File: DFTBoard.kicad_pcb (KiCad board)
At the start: 8 copper layers, 148.5 x 62 mm, 294 parts, among them CON1 AVR-JTAG-10, J1 PJ-102A, J2 AUDIO JACK, J3 AUDIO JACK, J4 AUDIO JACK, J5 JACK_TRS_4PINS, J6 USB_A, J7 USB_B, J8 Micro_SD_Card_Det, J9 HDMI_A, Q1 IRLML2502, Q10 IRLML2502, Q2 IRLML2502, Q3 IRLML2502, Q4 IRLML2502, Q5 IRLML2502, Q6 IRLML2502, Q7 IRLML2502, Q8 IRLML2502, Q9 IRLML2502, SW1 TL6215RF200BDT, U1 LM3880, U10 USB3320, U11 MIC2025-1YMM, U12 USB3320, U13 VL53L0X, U14 APDS-9960, U15 MT41K256M16HA-125_E, U16 MT41K256M16HA-125_E, U17 FTDITypeUART, U18 ABRACON-ASDMB, U19 S25FL256SAGNFI001, U2 LM3880, U20 xc7z020clg484, U3 SC189 - 1.0V, U4 SC189 - 3.3V, U5 TLV62080DSGx, U6 LM1085-5.0, U7 SC189 - 1.8V, U8 TPS51200DRCR, U9 TLV320AIC3104, Y1 ABM3-24.000MHZ-D2Y-T, Y2 ABM3-24.000MHZ-D2Y-T

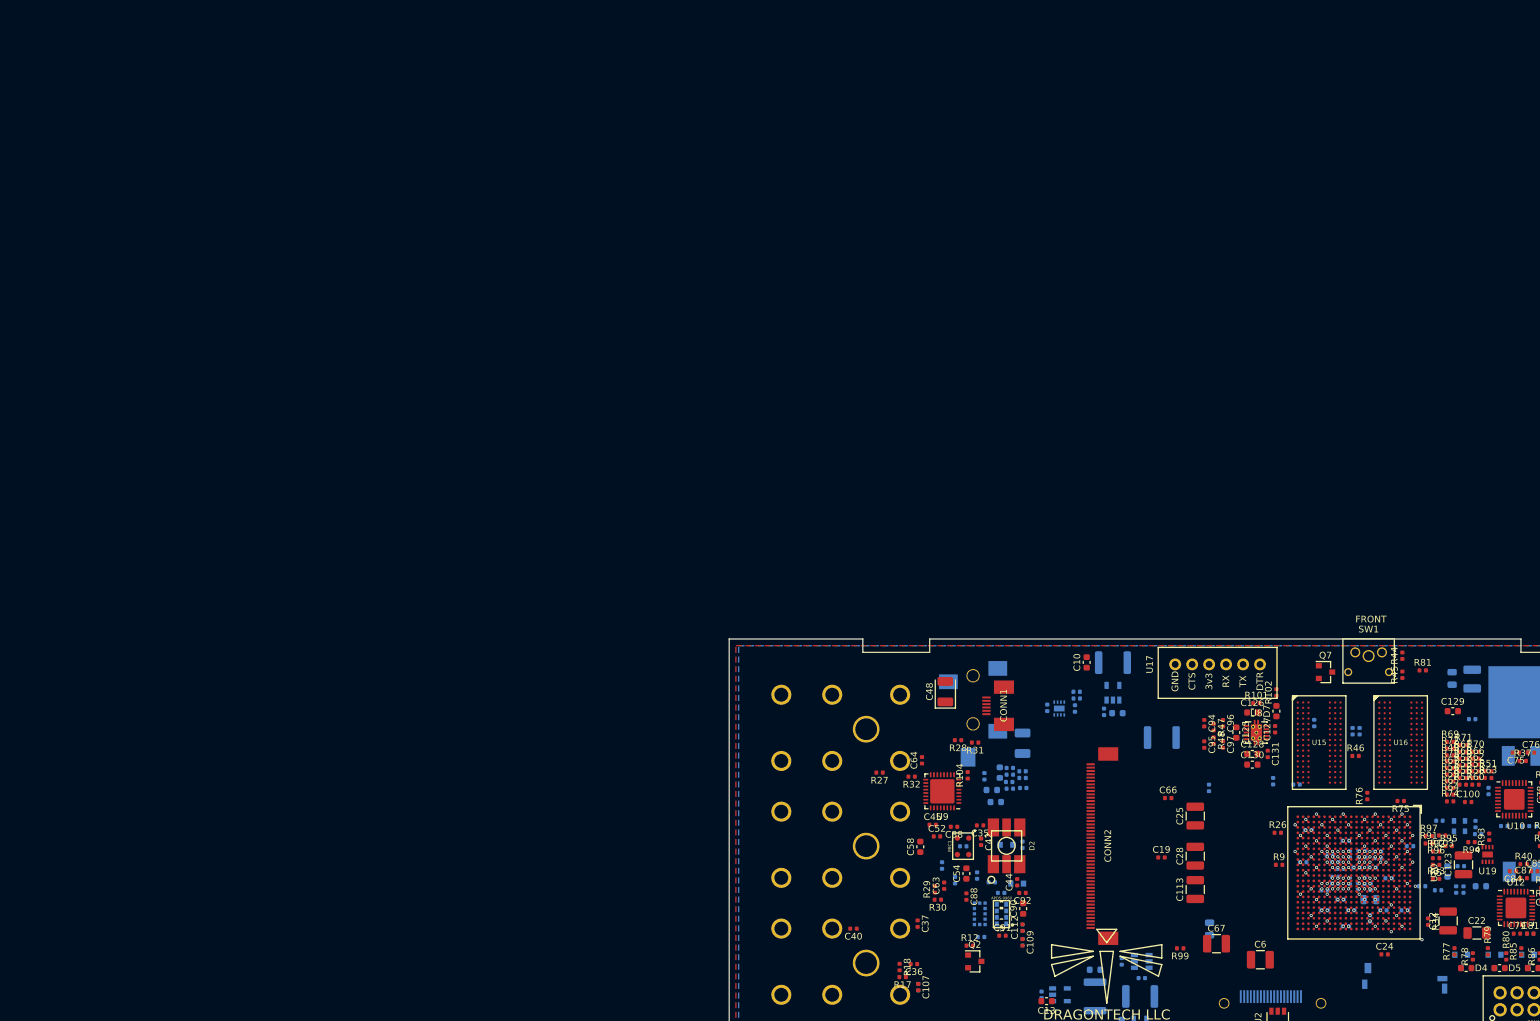
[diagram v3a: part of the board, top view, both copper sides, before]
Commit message: all DDR data signals routed, routing address
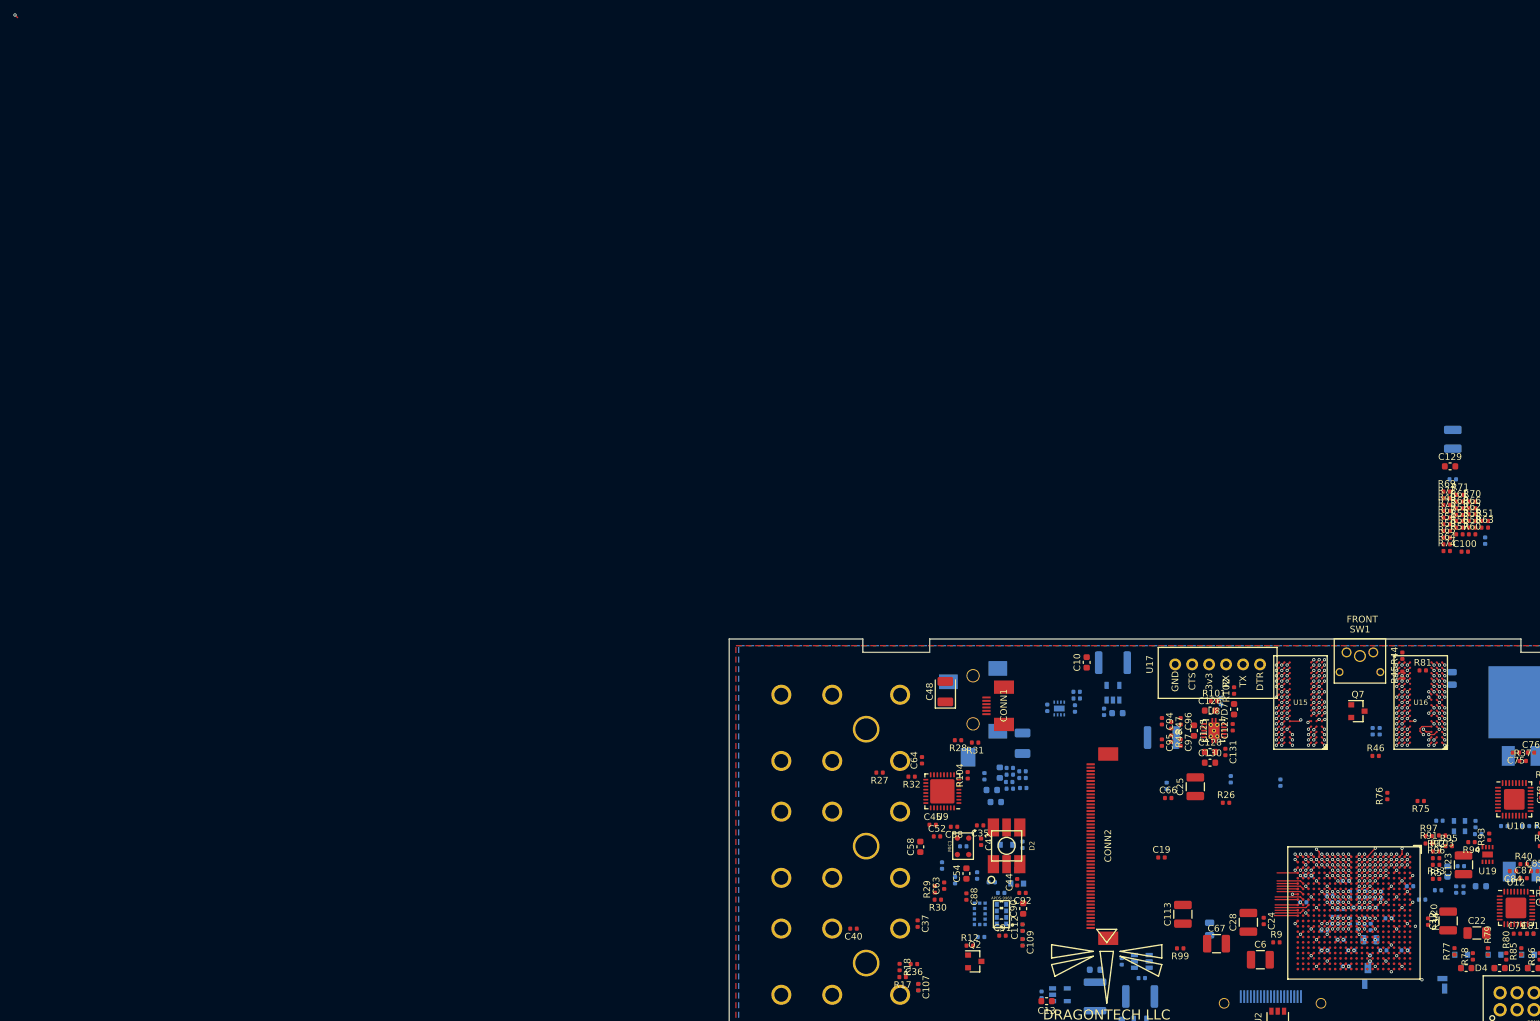
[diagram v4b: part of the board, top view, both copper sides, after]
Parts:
- moved C100 37.5 mm to (216.6, 79.9)
- moved C70 37.5 mm to (219.6, 78.3)
- moved R49 37.5 mm to (213.9, 72.9)
- moved R51 37.5 mm to (219.6, 75.3)
- moved R52 37.5 mm to (215.8, 74.4)
- moved R53 37.5 mm to (215.8, 75.3)
- moved R54 37.5 mm to (213.9, 75.8)
- moved R55 37.5 mm to (217.7, 75.3)
- moved R56 37.5 mm to (215.8, 76.3)
- moved R57 37.5 mm to (215.8, 77.3)
- moved R58 37.5 mm to (217.7, 76.3)
- moved R59 37.5 mm to (213.9, 76.8)
- moved R60 37.5 mm to (217.7, 77.3)
- moved R61 37.5 mm to (215.8, 72.4)
- moved R62 37.5 mm to (217.7, 74.3)
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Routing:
- net DDR3_CS#: track 0.00 -> 66.2 mm, vias 0 -> 3
- net DDR3_ODT: track 0.00 -> 65.1 mm, vias 0 -> 3
- net DDR3_RAS#: track 0.00 -> 58.5 mm, vias 0 -> 3
- net DDR3_DQ7: track 0.00 -> 49.0 mm, vias 0 -> 2
- net DDR3_WE#: track 0.00 -> 40.7 mm, vias 0 -> 3
- net DDR3_A13: track 0.00 -> 38.5 mm, vias 0 -> 3
- net DDR3_DRST#: track 0.00 -> 37.2 mm, vias 0 -> 3
- net DDR3_DQ6: track 0.00 -> 35.9 mm, vias 0 -> 2
- net DDR3_CK_N: track 0.00 -> 35.8 mm, vias 0 -> 3
- net DDR3_DQ4: track 0.00 -> 35.7 mm, vias 0 -> 2
- net DDR3_A0: track 0.00 -> 35.3 mm, vias 0 -> 3
- net DDR3_DQ20: track 0.00 -> 34.7 mm, vias 0 -> 2
- net DDR3_A5: track 0.00 -> 34.6 mm, vias 0 -> 3
- net DDR3_CK_P: track 0.00 -> 33.9 mm, vias 0 -> 3
- net DDR3_A2: track 0.00 -> 33.6 mm, vias 0 -> 3
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- added copper zone on SIGNAL1, net +1V8
- added copper zone on B.Cu, net GND
- removed copper zone on 1V8, net +1V8
- removed copper zone on B.Cu, net +3V3
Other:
- net class DDR_Differential: trace_width 0.13 -> 0.102
- net class DDR_Single: trace_width 0.13 -> 0.102
- net class Default: trace_width 0.13 -> 0.102
- net class HDMI: trace_width 0.13 -> 0.102
- net class Power: trace_width 0.13 -> 0.102

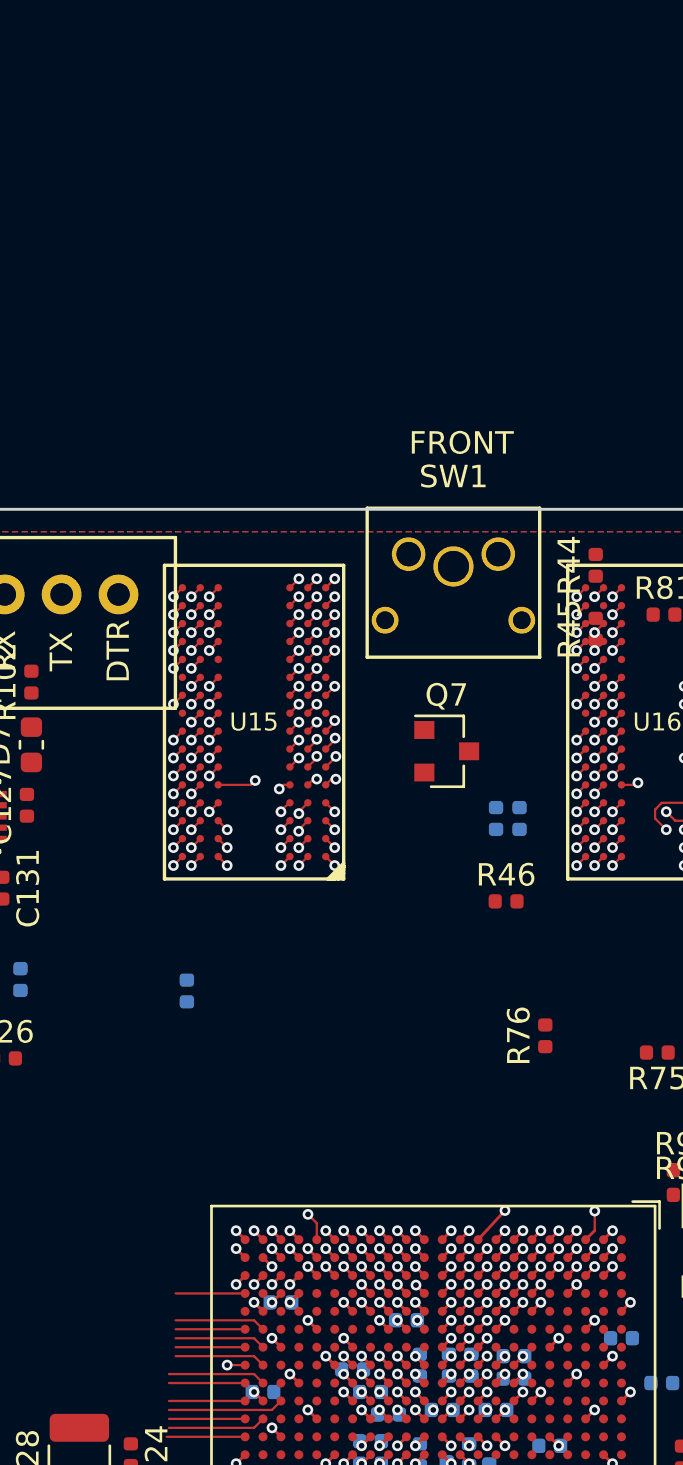
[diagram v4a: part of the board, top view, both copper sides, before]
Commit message: DDR: data lines are set, address lines are f'd. gonna try routing from the right
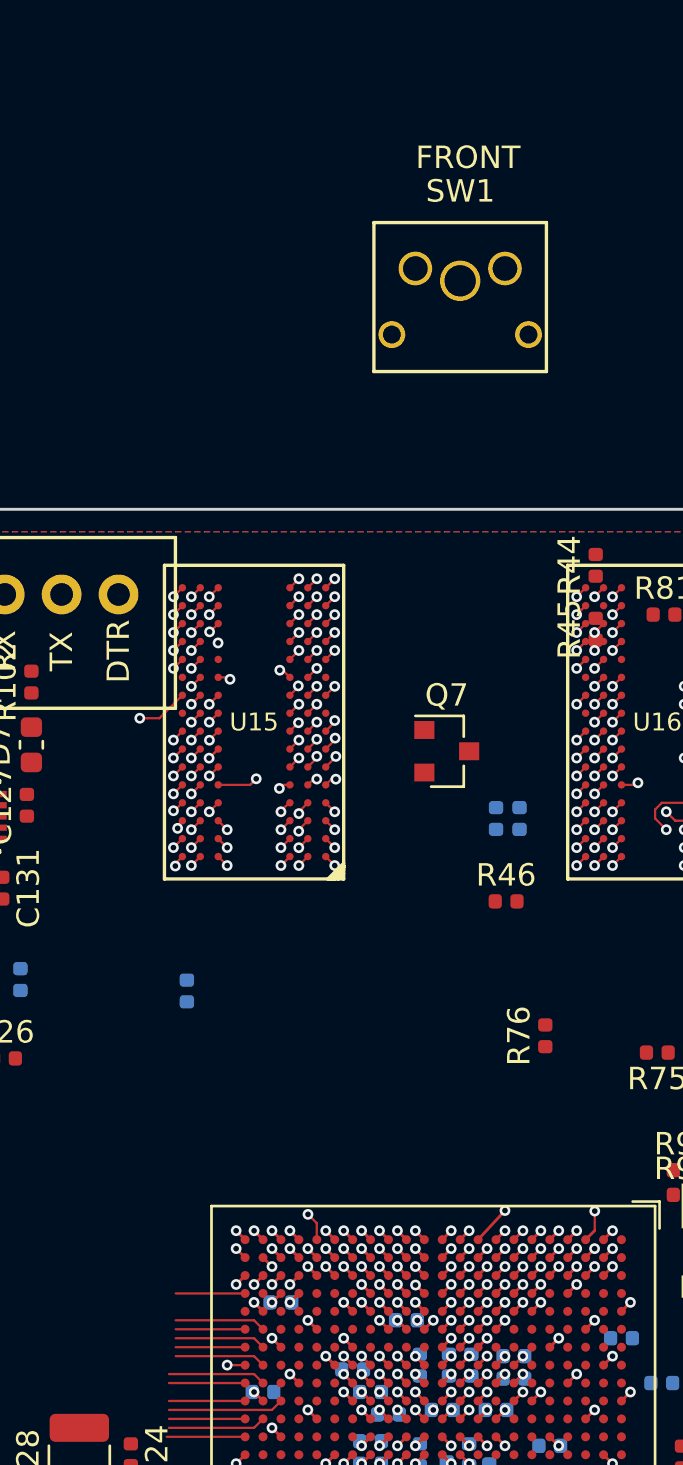
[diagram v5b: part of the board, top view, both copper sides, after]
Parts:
- moved SW1 12.8 mm to (201.2, 80.2)
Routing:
- net DDR3_A11: track 1.70 -> 46.8 mm
- net DDR3_A4: track 1.70 -> 44.6 mm
- net DDR3_A12: track 13.7 -> 53.6 mm
- net DDR3_A6: track 1.13 -> 39.9 mm
- net DDR3_A8: track 1.70 -> 38.7 mm
- net DDR3_BA0: track 21.5 -> 58.4 mm
- net DDR3_A9: track 21.1 -> 58.0 mm
- net DDR3_A7: track 21.2 -> 56.8 mm
- net DDR3_BA2: track 20.1 -> 55.4 mm, vias 2 -> 3
- net DDR3_A2: track 33.6 -> 58.7 mm
- net DDR3_A5: track 34.6 -> 59.0 mm
- net DDR3_A14: track 15.0 -> 38.5 mm
- net DDR3_A3: track 33.5 -> 56.1 mm
- net DDR3_A10: track 12.7 -> 35.1 mm
- net DDR3_A13: track 38.5 -> 60.8 mm
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
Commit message: all ddr address lines routed ???
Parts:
- moved R81 10.4 mm to (220.7, 97.2)
- moved R45 4.84 mm to (202.5, 97.4)
- moved C7 4.58 mm to (218.5, 96.3)
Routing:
- net DDR3_CAS#: track 19.8 -> 61.7 mm
- net DDR3_A6: track 39.9 -> 75.1 mm, vias 2 -> 3
- net DDR3_CKE: track 31.4 -> 64.3 mm
- net DDR3_A14: track 38.5 -> 67.1 mm
- net DDR3_A10: track 35.1 -> 62.8 mm
- net DDR3_A8: track 38.7 -> 65.7 mm
- net DDR3_BA1: track 36.4 -> 61.1 mm
- net DDR3_A11: track 46.8 -> 71.0 mm
- net DDR3_A1: track 38.9 -> 60.1 mm
- net DDR3_CK_N: track 35.8 -> 56.5 mm
- net DDR3_CK_P: track 34.6 -> 54.6 mm
- net DDR3_A4: track 44.6 -> 62.8 mm
- net DDR3_WE#: track 47.7 -> 62.6 mm
- net DDR3_A12: track 53.6 -> 66.9 mm
- net DDR3_A5: track 59.0 -> 45.8 mm
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
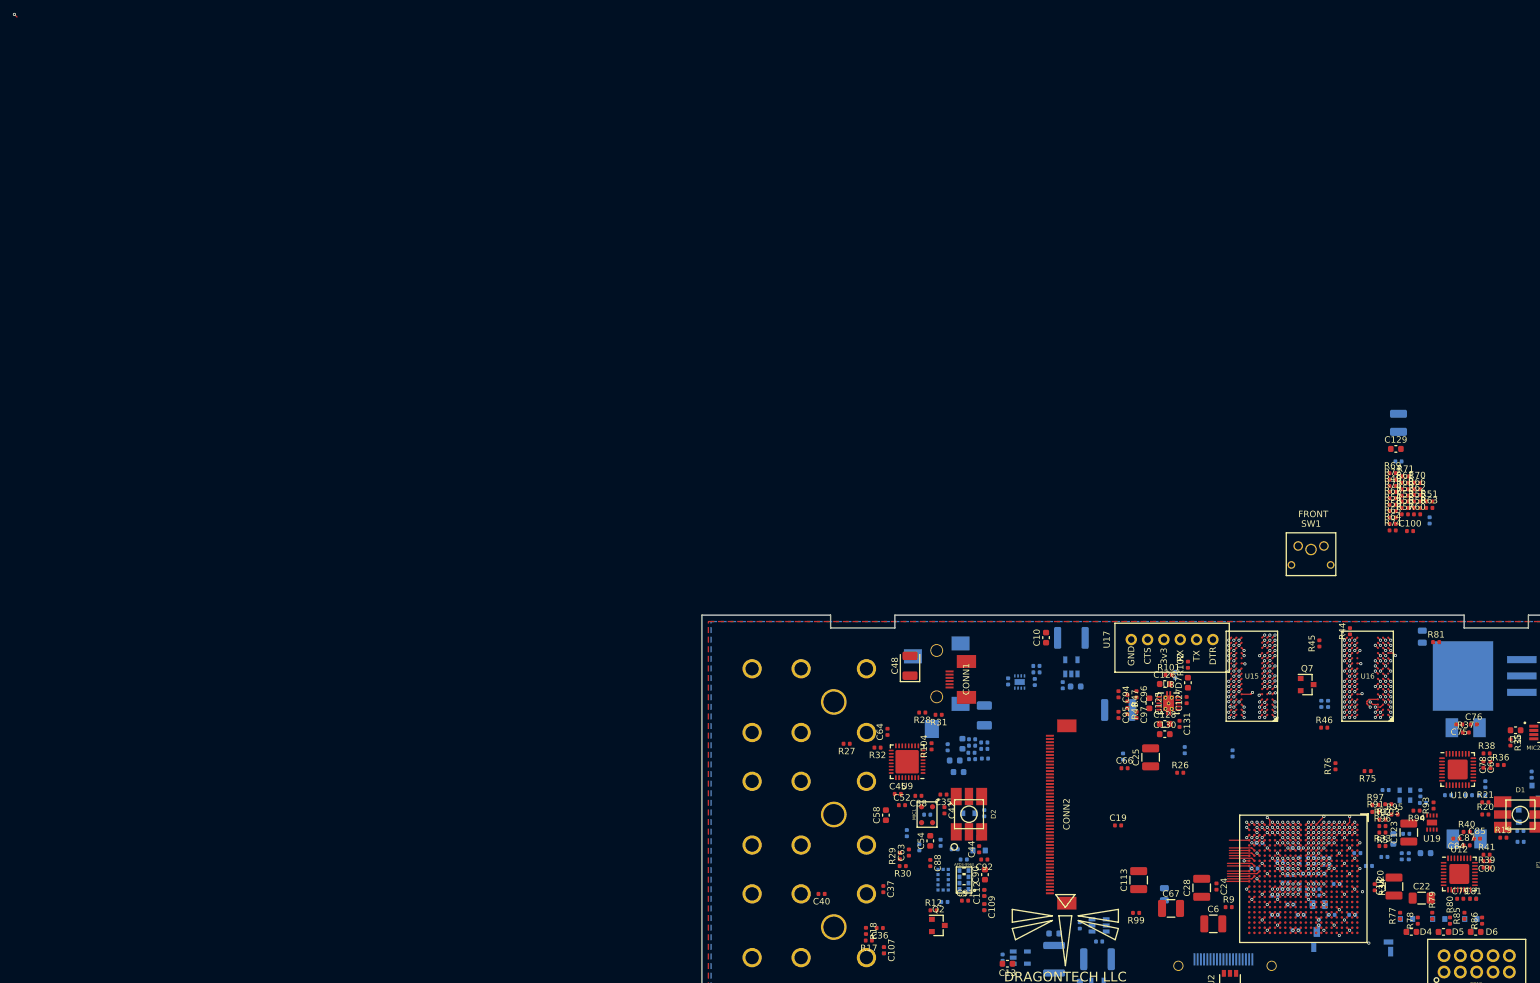
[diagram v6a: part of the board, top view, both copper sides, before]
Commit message: finished DDR pinswaps, about to reposition chips closer to each other, and closer to the FPGA
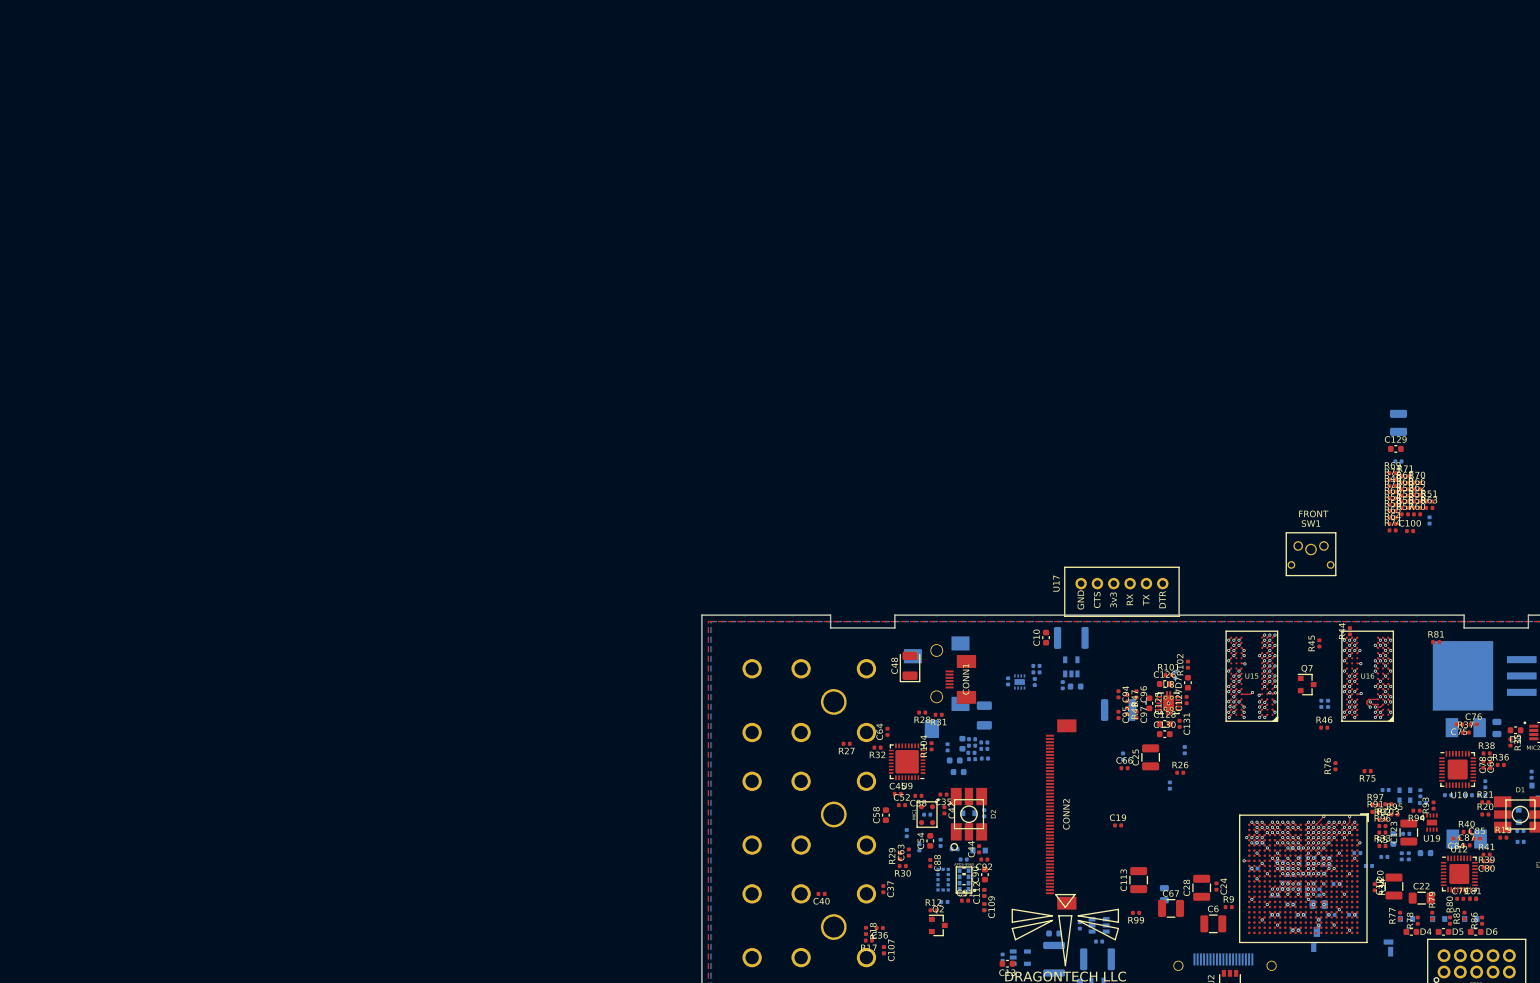
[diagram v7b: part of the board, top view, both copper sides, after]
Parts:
- moved C7 18.3 mm to (230.1, 110.5)
- moved U17 11.7 mm to (171.8, 88.1)
- moved C103 11.0 mm to (179.2, 119.5)
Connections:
- U15 pad A2: DDR3_DQ29 -> DDR3_DQ31
- U15 pad A3: DDR3_DQ31 -> DDR3_DQ26
- U15 pad C2: DDR3_DQ27 -> DDR3_DQ25
- U15 pad C3: DDR3_DQ25 -> DDR3_DQ27
- U15 pad C8: DDR3_DQ26 -> DDR3_DQ29
- U15 pad E3: DDR3_DQ16 -> DDR3_DQ17
- U15 pad F2: DDR3_DQ18 -> DDR3_DQ16
- U15 pad F7: DDR3_DQ17 -> DDR3_DQ19
- U15 pad F8: DDR3_DQ19 -> DDR3_DQ21
- U15 pad H3: DDR3_DQ20 -> DDR3_DQ18
- U15 pad H7: DDR3_DQ23 -> DDR3_DQ20
- U15 pad H8: DDR3_DQ21 -> DDR3_DQ23
- U16 pad A2: DDR3_DQ13 -> DDR3_DQ8
- U16 pad A3: DDR3_DQ15 -> DDR3_DQ9
- U16 pad A7: DDR3_DQ12 -> DDR3_DQ13
- U16 pad B8: DDR3_DQ14 -> DDR3_DQ15
- U16 pad C2: DDR3_DQ11 -> DDR3_DQ14
- U16 pad C3: DDR3_DQ9 -> DDR3_DQ11
- U16 pad D7: DDR3_DQ8 -> DDR3_DQ12
- U16 pad F7: DDR3_DQ1 -> DDR3_DQ4
- U16 pad F8: DDR3_DQ3 -> DDR3_DQ7
- U16 pad G2: DDR3_DQ6 -> DDR3_DQ1
- U16 pad H3: DDR3_DQ4 -> DDR3_DQ3
- U16 pad H7: DDR3_DQ7 -> DDR3_DQ6
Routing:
- net DDR3_DQ18: track 34.3 -> 0.56 mm, vias 2 -> 1
- net DDR3_DQ16: track 21.9 -> 0.00 mm, vias 2 -> 0
- net +1V35: track 26.9 -> 5.69 mm, vias 45 -> 10
- net DDR3_DQ7: track 49.0 -> 31.5 mm
- net DDR3_DQ3: track 17.7 -> 33.8 mm
- net DDR3_A13: track 65.7 -> 77.0 mm
- net DDR3_A11: track 71.0 -> 81.8 mm
- net DDR3_DRST#: track 62.9 -> 72.2 mm
- net DDR3_A9: track 66.2 -> 75.1 mm
- net DDR3_DQ6: track 35.9 -> 44.0 mm
- net DDR3_DQ9: track 29.5 -> 21.8 mm
- net DDR3_A7: track 65.1 -> 72.1 mm
- net DDR3_DQ11: track 22.1 -> 28.4 mm
- net DDR3_DQ1: track 24.7 -> 31.0 mm
- net DDR3_DQ12: track 22.3 -> 28.4 mm
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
